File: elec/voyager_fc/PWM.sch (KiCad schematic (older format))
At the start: 52 parts

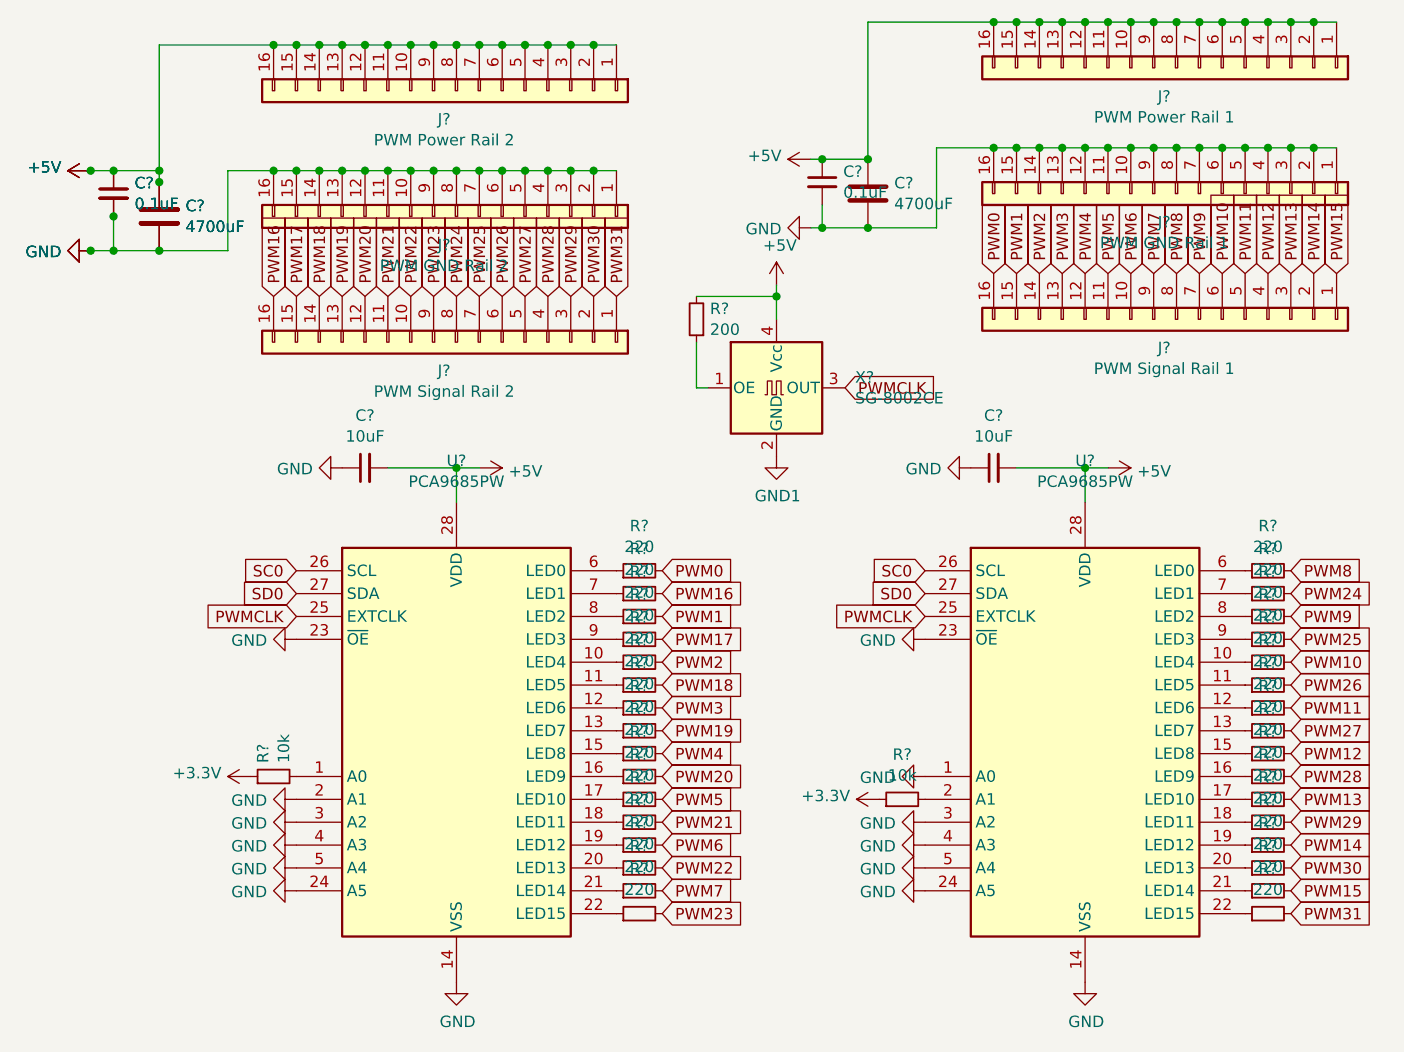
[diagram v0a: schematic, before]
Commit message: Place all components and start route
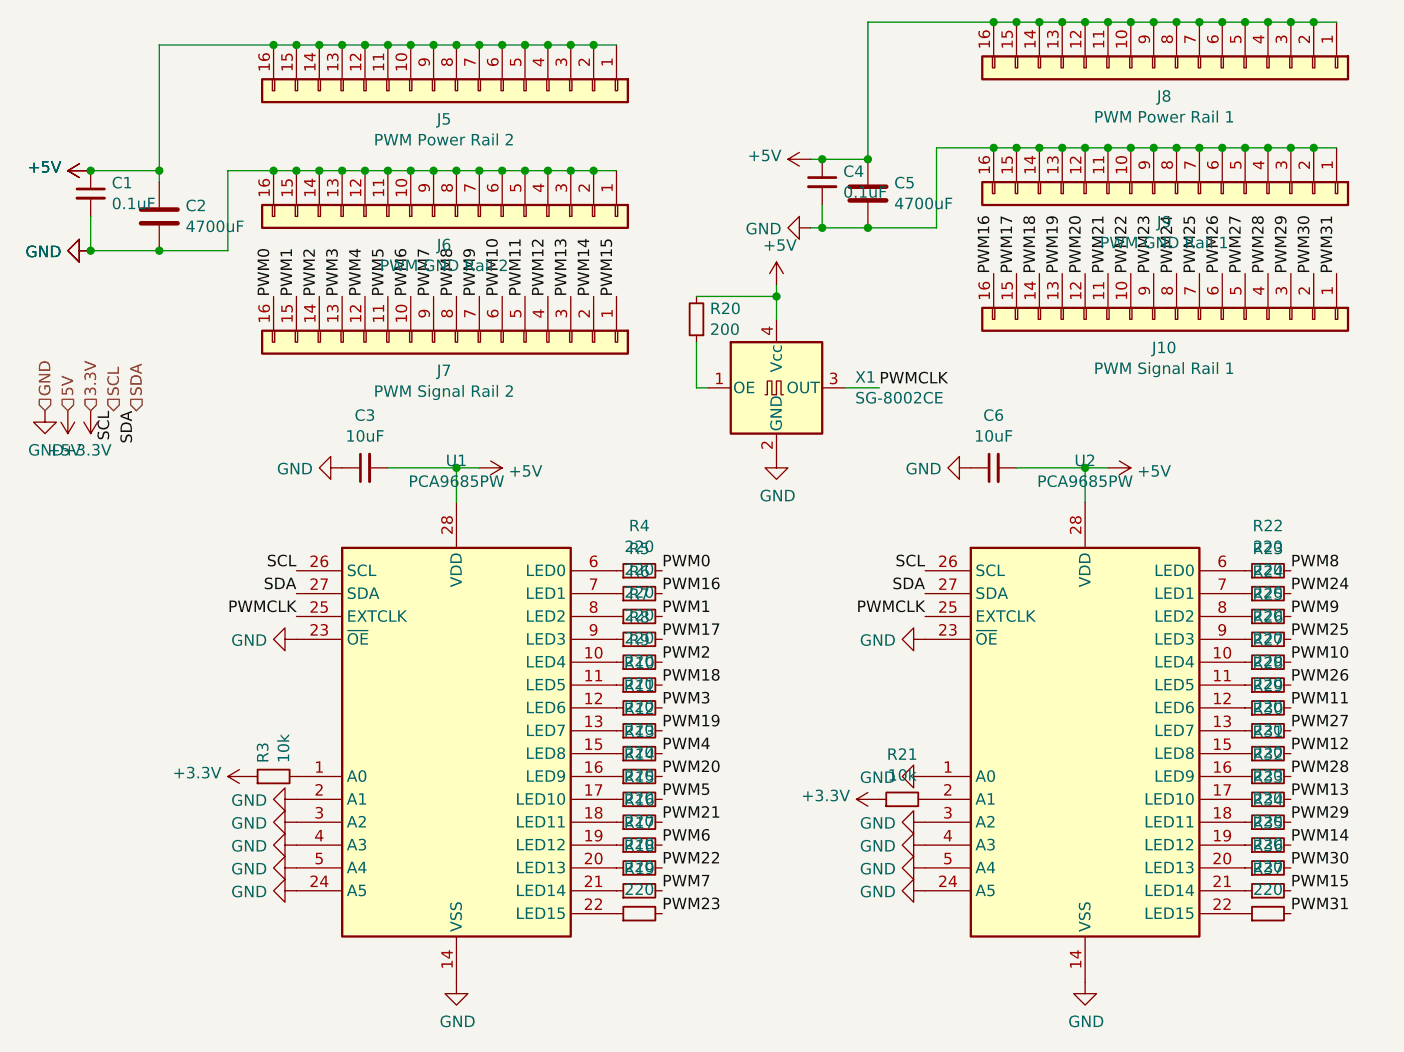
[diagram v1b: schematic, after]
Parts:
- removed C?: 4700uF, Capacitor_THT:CP_Radial_D10.0mm_P5.00mm, symbol Device:C
- removed C?: 0.1uF, Capacitor_SMD:C_0603_1608Metric, symbol Device:C_Small
- C1, C4: renamed from C?; footprint Capacitor_SMD:C_0603_1608Metric -> Capacitor_SMD:C_0402_1005Metric
- C3, C6: renamed from C?; footprint Capacitor_SMD:C_0805_2012Metric -> Capacitor_SMD:C_0603_1608Metric
- R10, R11, R12, R13, R14, R15, R16, R17, R18, R19, R20, R22, R23, R24, R25, R26, R27, R28, R29, R30, R31, R32, R33, R34, R35, R36, R37, R4, R5, R6, R7, R8, R9: renamed from R?; footprint Resistor_SMD:R_0603_1608Metric -> Resistor_SMD:R_0402_1005Metric
- gave numbers to parts that had none: 13
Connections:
- net GND1 is gone; now on net GND: X1.2 (GND)
- net PWM0: now also J7.16 (Pin_16); no longer J10.16 (Pin_16)
- net PWM1: now also J7.15 (Pin_15); no longer J10.15 (Pin_15)
- net PWM10: now also J7.6 (Pin_6); no longer J10.6 (Pin_6)
- net PWM11: now also J7.5 (Pin_5); no longer J10.5 (Pin_5)
- net PWM12: now also J7.4 (Pin_4); no longer J10.4 (Pin_4)
- net PWM13: now also J7.3 (Pin_3); no longer J10.3 (Pin_3)
- net PWM14: now also J7.2 (Pin_2); no longer J10.2 (Pin_2)
- net PWM15: now also J7.1 (Pin_1); no longer J10.1 (Pin_1)
- net PWM16: now also J10.16 (Pin_16); no longer J7.16 (Pin_16)
- net PWM17: now also J10.15 (Pin_15); no longer J7.15 (Pin_15)
- net PWM18: now also J10.14 (Pin_14); no longer J7.14 (Pin_14)
- net PWM19: now also J10.13 (Pin_13); no longer J7.13 (Pin_13)
- net PWM2: now also J7.14 (Pin_14); no longer J10.14 (Pin_14)
- net PWM20: now also J10.12 (Pin_12); no longer J7.12 (Pin_12)
- net PWM21: now also J10.11 (Pin_11); no longer J7.11 (Pin_11)
- net PWM22: now also J10.10 (Pin_10); no longer J7.10 (Pin_10)
- net PWM23: now also J10.9 (Pin_9); no longer J7.9 (Pin_9)
- net PWM24: now also J10.8 (Pin_8); no longer J7.8 (Pin_8)
- net PWM25: now also J10.7 (Pin_7); no longer J7.7 (Pin_7)
- net PWM26: now also J10.6 (Pin_6); no longer J7.6 (Pin_6)
- net PWM27: now also J10.5 (Pin_5); no longer J7.5 (Pin_5)
- net PWM28: now also J10.4 (Pin_4); no longer J7.4 (Pin_4)
- net PWM29: now also J10.3 (Pin_3); no longer J7.3 (Pin_3)
- net PWM3: now also J7.13 (Pin_13); no longer J10.13 (Pin_13)
- net PWM30: now also J10.2 (Pin_2); no longer J7.2 (Pin_2)
- net PWM31: now also J10.1 (Pin_1); no longer J7.1 (Pin_1)
- net PWM4: now also J7.12 (Pin_12); no longer J10.12 (Pin_12)
- net PWM5: now also J7.11 (Pin_11); no longer J10.11 (Pin_11)
- net PWM6: now also J7.10 (Pin_10); no longer J10.10 (Pin_10)
- net PWM7: now also J7.9 (Pin_9); no longer J10.9 (Pin_9)
- net PWM8: now also J7.8 (Pin_8); no longer J10.8 (Pin_8)
- net PWM9: now also J7.7 (Pin_7); no longer J10.7 (Pin_7)
- net SC0 renamed SCL
- net SD0 renamed SDA
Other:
- moved on the sheet: C1
